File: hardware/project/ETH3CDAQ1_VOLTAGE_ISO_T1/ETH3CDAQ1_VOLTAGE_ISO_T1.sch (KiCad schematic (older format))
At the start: 80 parts, among them J101 GMSTB2,5/2-GF-7,62, J102 Conn_02x10_Odd_Even, U101 DG211, U102 DG419xY, U103 LT3032, U104 OPA140, U105 ISO124, U106 ADuM5410, U107 DCP020515DU, U108 OPA237_SOT23, U109 LT3032-15, U110 74LVC1GU04DRL, U111 74LVC1GU04DRL, U112 74LVC1GU04DRL, U113 24LC08B-E/MS, U114 TXB0104PW, U115 PCA9557PW

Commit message: Voltage module done.
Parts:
- added R25: 10k, Resistor_SMD:R_0603_1608Metric_Pad0.98x0.95mm_HandSolder, symbol Device:R
- added R26: 0, Resistor_SMD:R_0603_1608Metric_Pad0.98x0.95mm_HandSolder, symbol Device:R
- renumbered C101 to C1, C127 to C10, C128 to C11, C106 to C12, C107 to C13, C129 to C14, C130 to C15, C108 to C16, C109 to C17, C110 to C18, C111 to C19, C102 to C2, C112 to C20, C113 to C21, C114 to C22, C115 to C23, C116 to C24, C117 to C25, C118 to C26, C119 to C27, C120 to C28, C121 to C29, C103 to C3, C122 to C30, C104 to C4, C105 to C5, C123 to C6, C124 to C7, C125 to C8, C126 to C9, E101 to E1, FB101 to FB1, FB102 to FB2, FB103 to FB3, H101 to H1, H102 to H2, J101 to J1, J102 to J2, L101 to L1, R101 to R1, R110 to R10, R111 to R11, R112 to R12, R113 to R13, R114 to R14, R115 to R15, R116 to R16, R117 to R17, R118 to R18, R119 to R19, R102 to R2, R120 to R20, R121 to R21, R122 to R22, R123 to R23, R124 to R24, R103 to R3, R104 to R4, R105 to R5, R106 to R6, R107 to R7, R108 to R8, R109 to R9, RV101 to RV1, SYM101 to SYM1, U101 to U1, U110 to U10, U111 to U11, U112 to U12, U113 to U13, U114 to U14, U115 to U15, U102 to U2, U103 to U3, U104 to U4, U105 to U5, U106 to U6, U107 to U7, U108 to U8, U109 to U9
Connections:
- net +3V3: now also R25.1
- net IO_G1: now also R26.2
- net IO3: now reaches U15.10 (IO3)
- net IO3: now also U14.4 (A3); no longer U14.3 (A2)
- net IO4: now reaches U15.11 (IO4)
- net IO4: now also U14.3 (A2); no longer U14.4 (A3)
- net IO2: now reaches U14.5 (A4)
- net IO2: now also U15.9 (IO2); no longer U15.12 (IO5)
- net IO5: now reaches U14.2 (A1)
- net IO5: now also U15.12 (IO5); no longer U15.9 (IO2)
- net at U10.2, U14.13 (B1): now also R26.1
- net at U14.8 (OE): now also R25.2
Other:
- note added: "Connector"
- note added: "Digital IO"
- note added: "EEPROM\n"
- note added: "Isolated OP-Amp and low pass filter"
- note added: "Isolated digital IO side A"
- note added: "Isolated digital IO side B"
- note added: "Isolated power"
- note added: "Isolated power side A"
- note added: "Isolated power side B"
- note added: "Misc."
- note added: "Power"
- note added: "Voltage divider and PGA"
- moved on the sheet: C10, C11, C12, C13, C14, C15, C16, C17, C18, C2, C20, C21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

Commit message: PCB design
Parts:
- added C31: 10u, Capacitor_SMD:C_0603_1608Metric_Pad1.08x0.95mm_HandSolder, symbol Device:C
- added C32: 100n, Capacitor_SMD:C_0603_1608Metric_Pad1.08x0.95mm_HandSolder, symbol Device:C
- C14, C15: value 100n -> 10u
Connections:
- net +5V: now also C31.1, C32.1
- net GND: now also C31.2, C32.2
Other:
- moved on the sheet: C26, C27, C28, C29, FB2, FB3

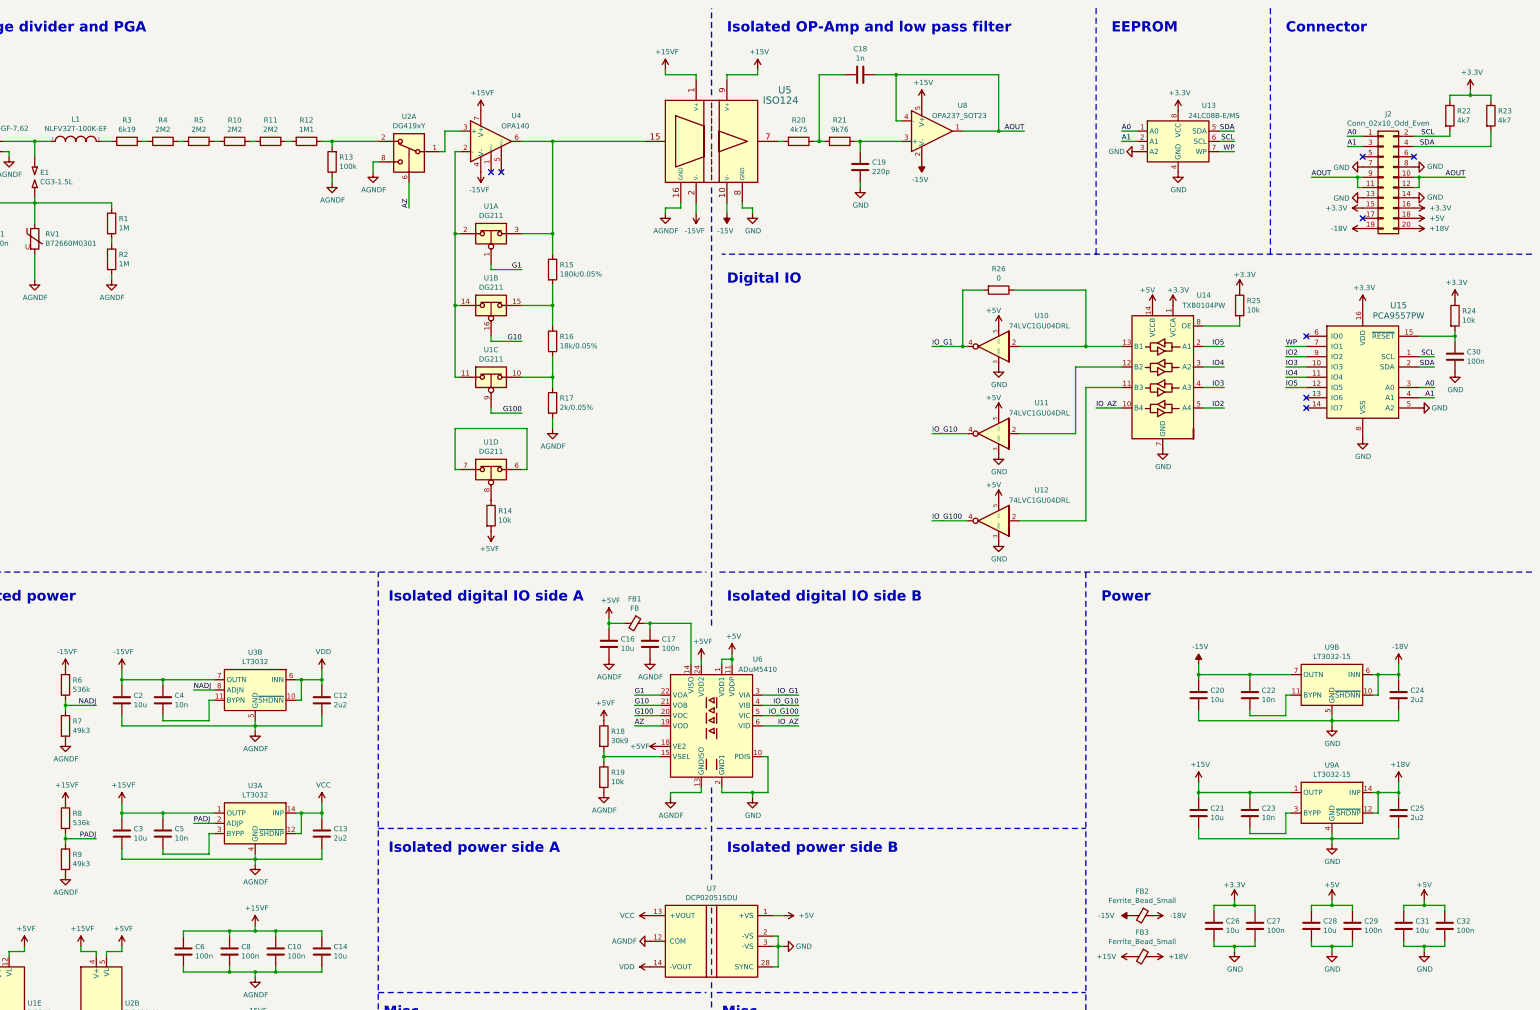
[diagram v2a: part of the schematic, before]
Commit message: Modification in PCBs. Created BOM files.
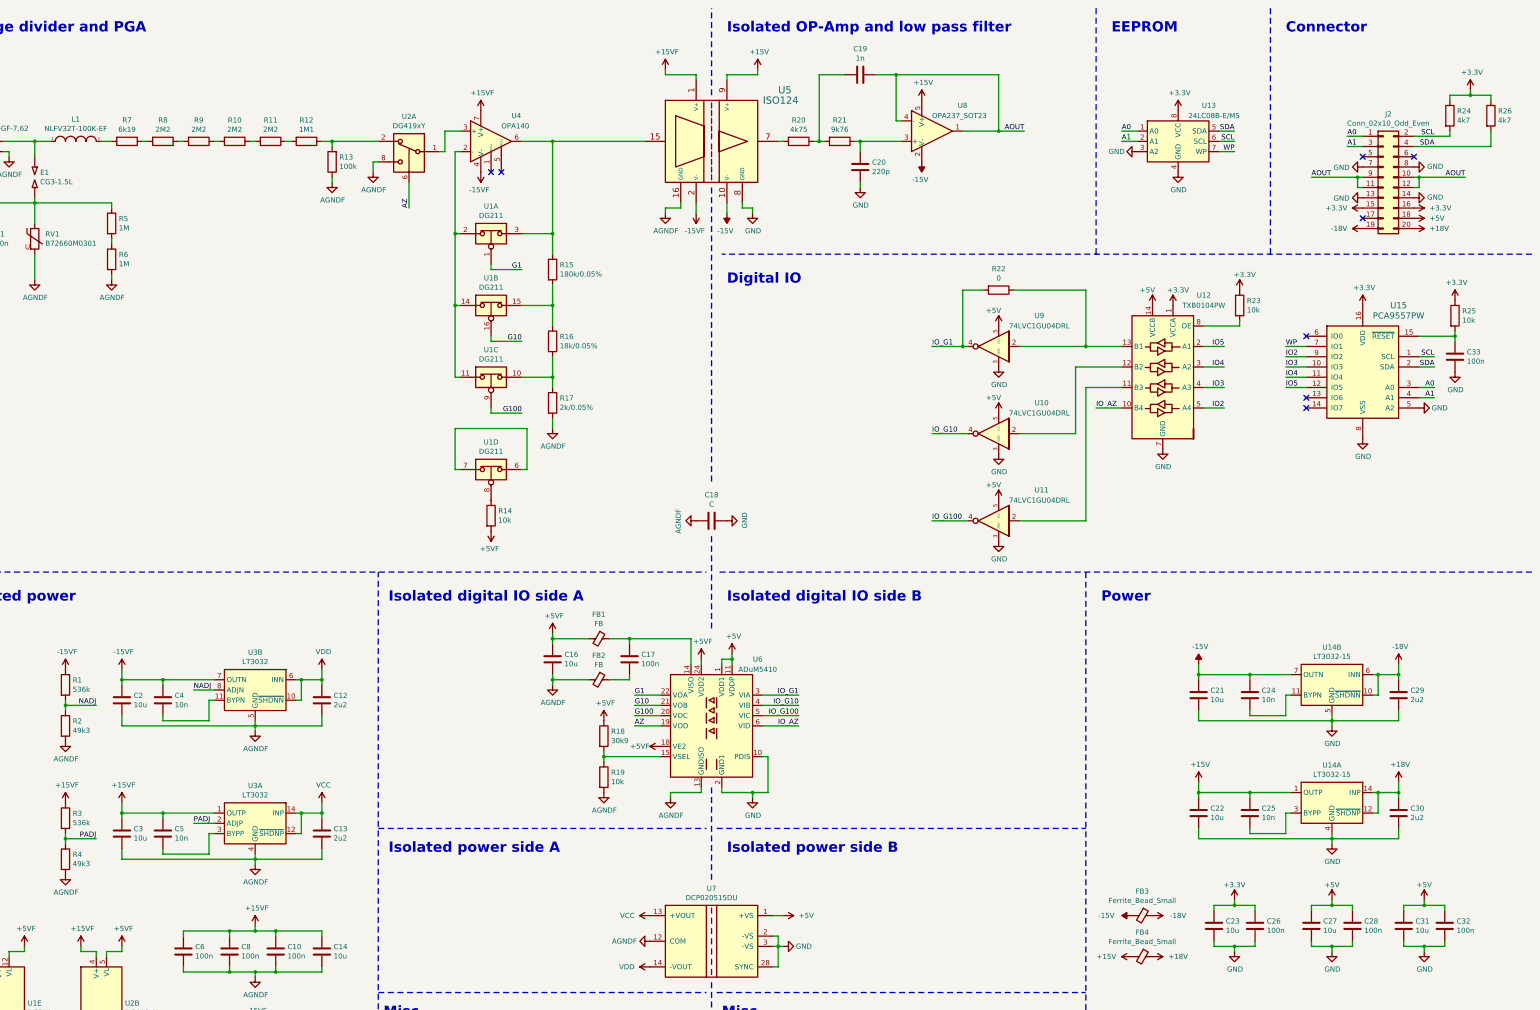
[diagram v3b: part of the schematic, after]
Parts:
- added C18: C, Capacitor_SMD:C_1812_4532Metric_Pad1.57x3.40mm_HandSolder, symbol Device:C
- added FB2: FB, Resistor_SMD:R_0603_1608Metric_Pad0.98x0.95mm_HandSolder, symbol Device:Ferrite_Bead_Small
- renumbered C18 to C19, C19 to C20, C20 to C21, C21 to C22, C26 to C23, C22 to C24, C23 to C25, C27 to C26, C28 to C27, C29 to C28, C24 to C29, C25 to C30, C30 to C33, FB2 to FB3, FB3 to FB4, R6 to R1, R7 to R2, R26 to R22, R25 to R23, R22 to R24, R24 to R25, R23 to R26, R8 to R3, R9 to R4, R1 to R5, R2 to R6, R3 to R7, R4 to R8, R5 to R9, U11 to U10, U12 to U11, U14 to U12, U9 to U14, U10 to U9
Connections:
- net AGNDF: now also C18.2, FB2.2; no longer C17.2
- net GND: now also C18.1
- new net: C17.2, FB2.1
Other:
- moved on the sheet: C16, C17, FB1

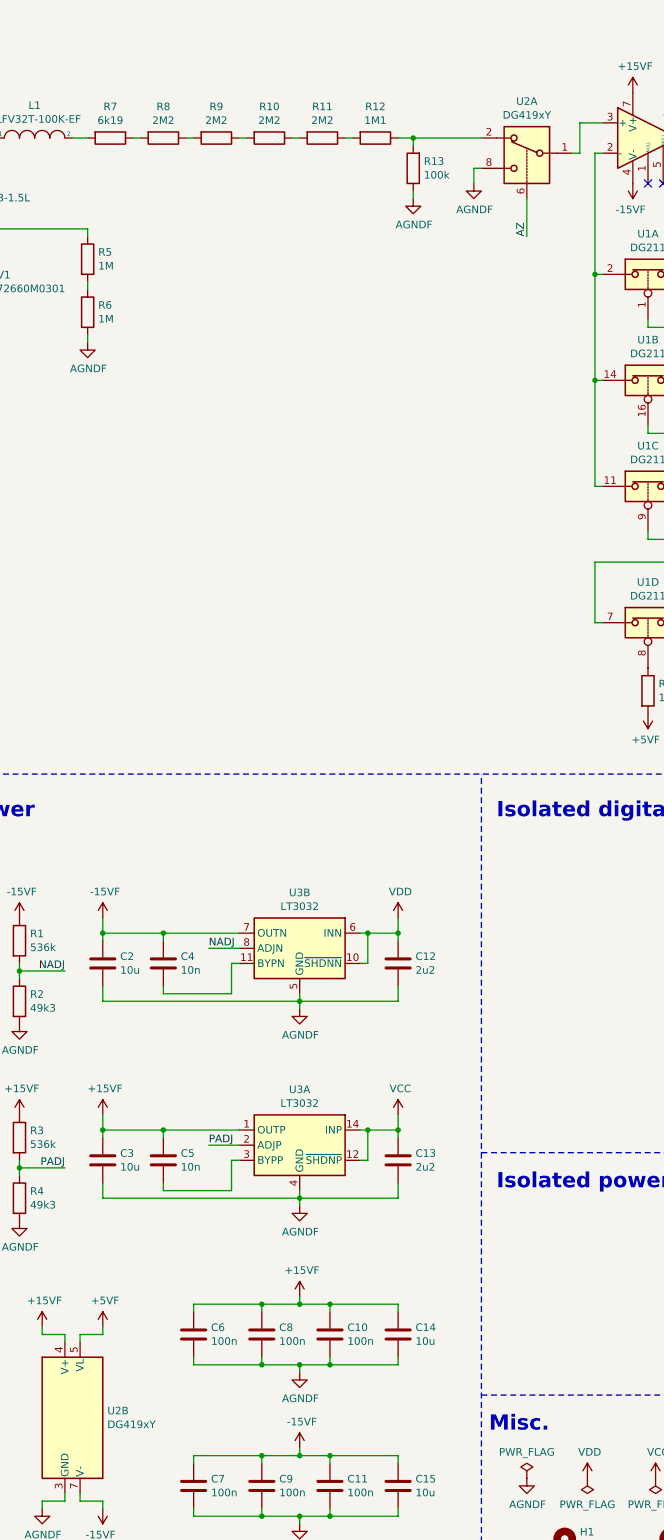
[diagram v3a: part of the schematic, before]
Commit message: Fixed mistake with DG419. Never use DG419Lxx variant.
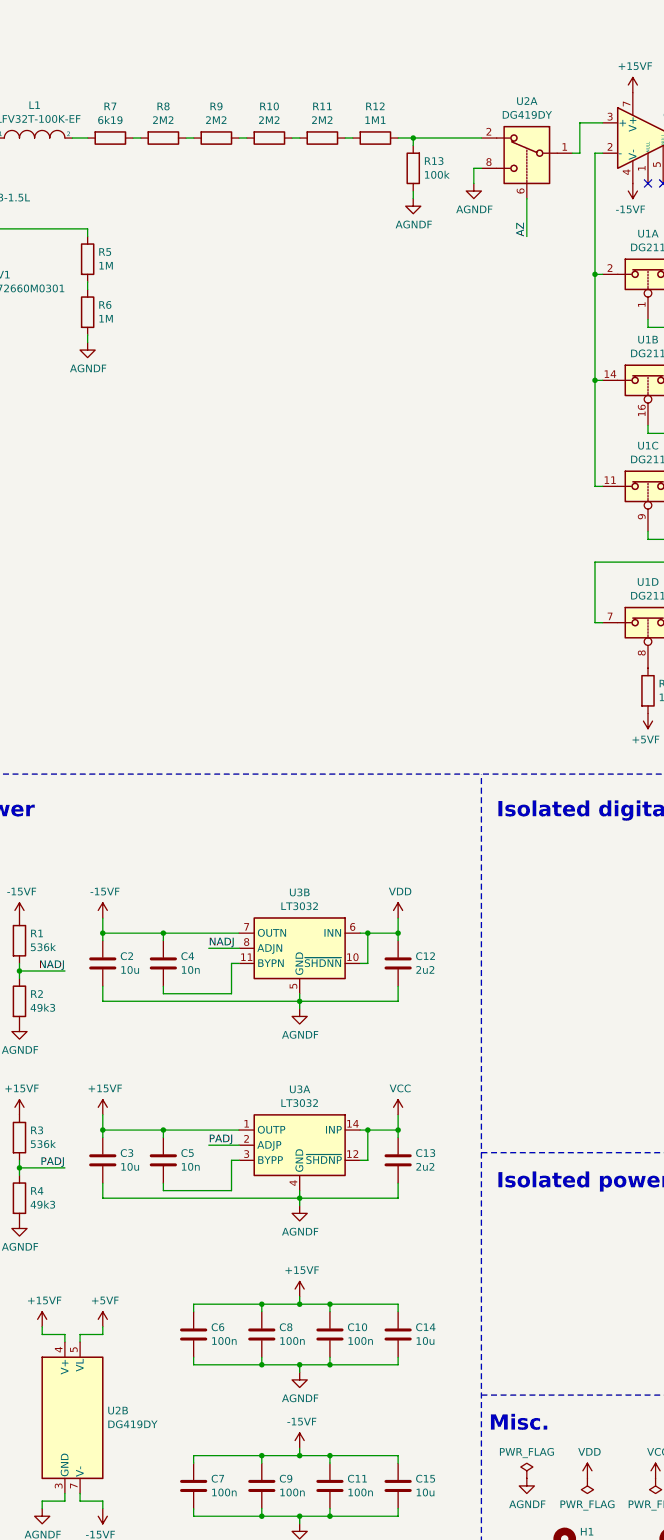
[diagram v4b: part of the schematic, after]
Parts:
- U2: value DG419xY -> DG419DY
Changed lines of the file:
@@
 P 5100 1800
 F 0 "U2" H 5100 2042 50  0000 C CNN
-F 1 "DG419xY" H 5100 1951 50  0000 C CNN
+F 1 "DG419DY" H 5100 1951 50  0000 C CNN
 F 2 "Package_SO:SOIC-8_3.9x4.9mm_P1.27mm" H 5100 1500 50  0001 C CNN
 F 3 "https://datasheets.maximintegrated.com/en/ds/DG417-DG419.pdf" H 5100 1800 50  0001 C CNN
@@
 P 2050 10250
 F 0 "U2" H 2330 10296 50  0000 L CNN
-F 1 "DG419xY" H 2330 10205 50  0000 L CNN
+F 1 "DG419DY" H 2330 10205 50  0000 L CNN
 F 2 "Package_SO:SOIC-8_3.9x4.9mm_P1.27mm" H 2050 9950 50  0001 C CNN
 F 3 "https://datasheets.maximintegrated.com/en/ds/DG417-DG419.pdf" H 2050 10250 50  0001 C CNN
